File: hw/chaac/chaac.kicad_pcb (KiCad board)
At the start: 2 copper layers, 68.5 x 45.5 mm, 61 parts, among them J1 windrain, J2 Conn_02x08_Odd_Even, J3 Conn_02x08_Odd_Even, J4 AM2315, J5 Battery, J6 Solar Panel, J7 UART, Q1 Q_PMOS_GSD, SW1 RST, SW2 RST, U1 MIC550X, U2 BMP280, U3 MCP73871

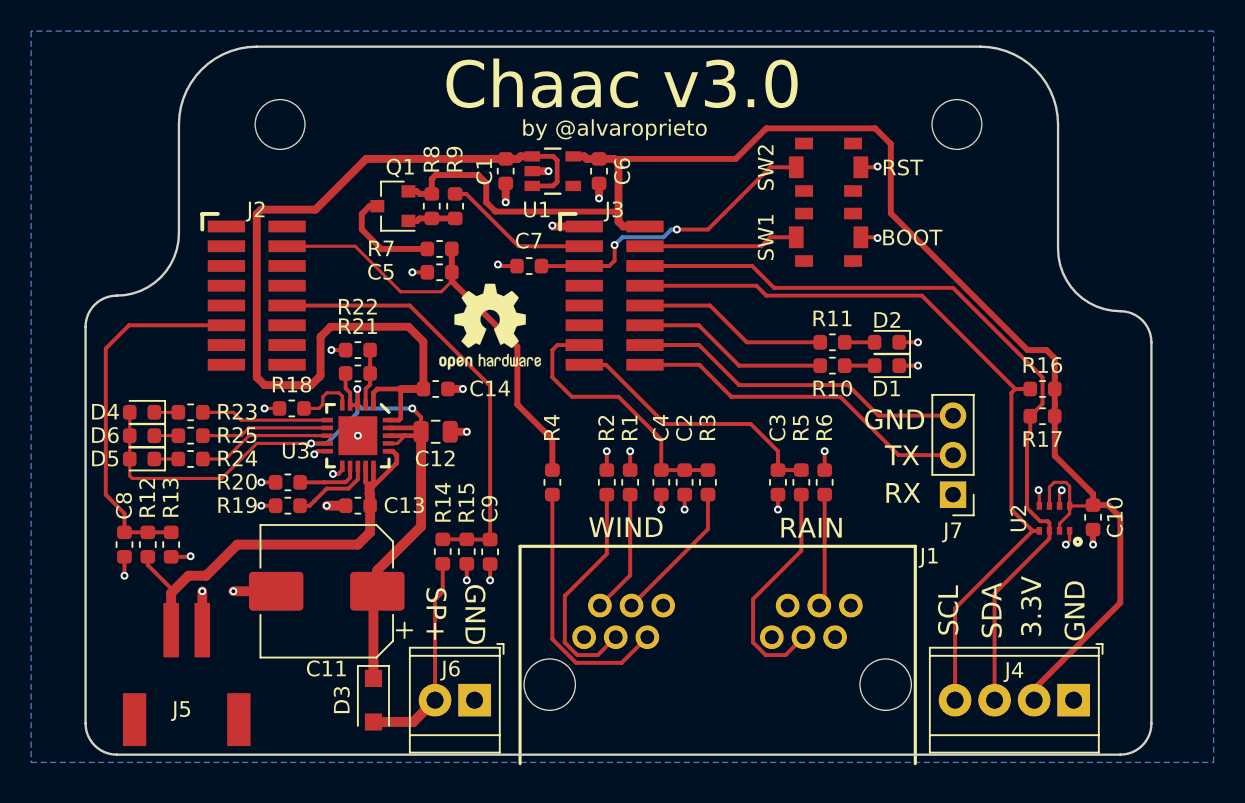
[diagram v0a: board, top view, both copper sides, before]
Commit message: Released chaac v3.1 to OSHPark
Moved NRF52 back into chaac pcb.
Removed external T/H connector, switched to BME280 for temp, humidity,
and pressure sensing.

Using RP-SMA connector for this version.
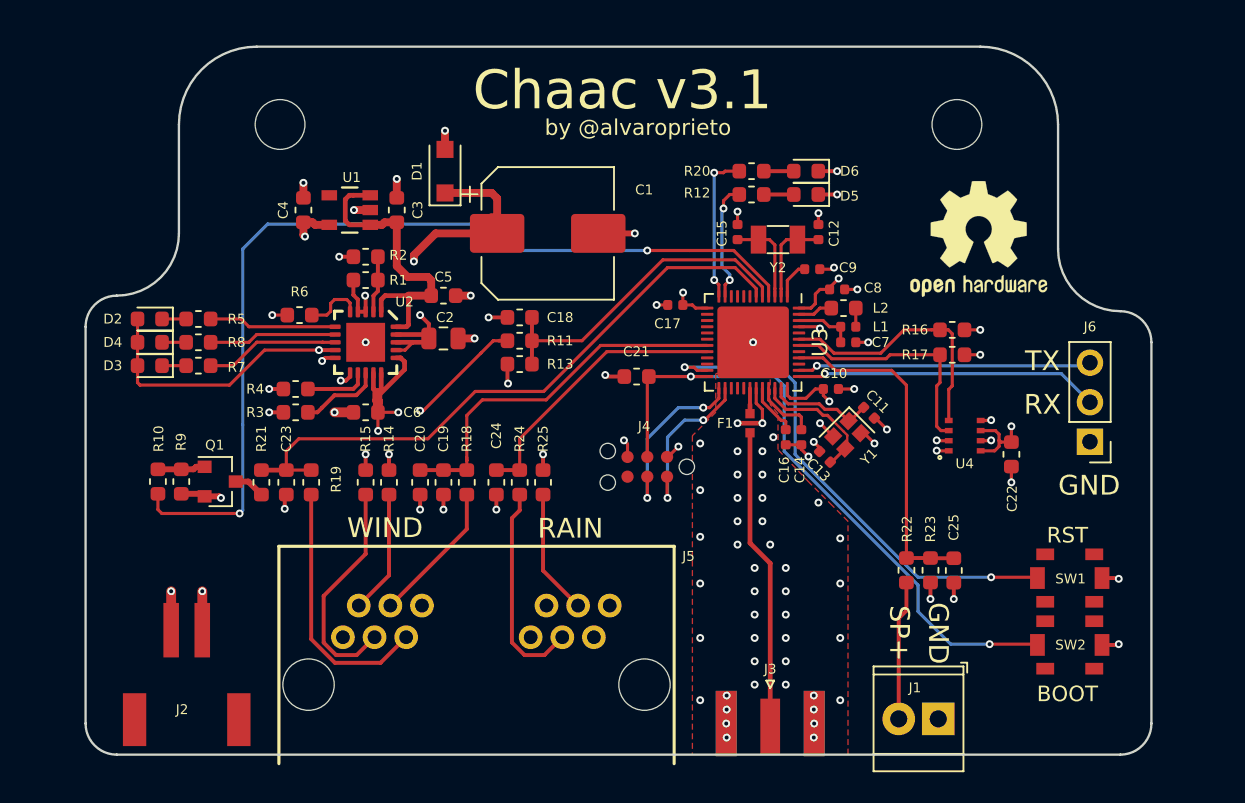
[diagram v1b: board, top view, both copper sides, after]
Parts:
- removed the J2 at (123.5, 91.0)
- removed the REF** at (138.5, 93.0)
- removed the U2 at (174.8, 105.3)
- added C10: 0.1uF, Capacitor_SMD:C_0402_1005Metric, F.Cu at (160.4, 97.0)
- added C11: 12pF, Capacitor_SMD:C_0402_1005Metric, F.Cu at (162.8, 98.5)
- added C12: 12pF, Capacitor_SMD:C_0402_1005Metric, F.Cu at (159.6, 86.9)
- added C13: 12pF, Capacitor_SMD:C_0402_1005Metric, F.Cu at (160.0, 101.4)
- added C14: 100pF, Capacitor_SMD:C_0402_1005Metric, F.Cu at (158.5, 100.1)
- added C15: 12pF, Capacitor_SMD:C_0402_1005Metric, F.Cu at (154.4, 86.9)
- added C16: DNP, Capacitor_SMD:C_0402_1005Metric, F.Cu at (157.5, 100.1)
- added C17: 0.1uF, Capacitor_SMD:C_0402_1005Metric, F.Cu at (150.4, 91.6)
- added C7: 1uF, Capacitor_SMD:C_0402_1005Metric, F.Cu at (161.5, 94.0)
- added C8: 4.7uF, Capacitor_SMD:C_0402_1005Metric, F.Cu at (160.8, 90.6)
- added C9: 0.1uF, Capacitor_SMD:C_0402_1005Metric, F.Cu at (159.2, 89.3)
- added F1: 2450FM07A0029T, alvarop:2450FM07A0029T, F.Cu at (155.2, 99.2)
- added L1: 15nH, Inductor_SMD:L_0402_1005Metric, F.Cu at (161.5, 93.0)
- added L2: 10uH, Inductor_SMD:L_0603_1608Metric, F.Cu at (161.2, 91.8)
- added REF**: OSHW-Logo2_9.8x8mm_SilkScreen, Symbol:OSHW-Logo2_9.8x8mm_SilkScreen, F.Cu at (169.9, 87.3)
- added U3: NRF52811-QFAA, alvarop:NRF52811-QFN48, F.Cu at (155.4, 94.0)
- added U4: BME280, alvarop:BME280, F.Cu at (169.0, 100.0)
- added Y1: 32MHz, Crystal:Crystal_SMD_2016-4Pin_2.0x1.6mm, F.Cu at (161.4, 99.9)
- added Y2: 32.768kHz, Crystal:Crystal_SMD_3215-2Pin_3.2x1.5mm, F.Cu at (157.0, 87.4)
- J3: value Conn_02x08_Odd_Even -> Conn_Coaxial; footprint alvarop:20021121-00016C4LF -> Connector_Coaxial:SMA_Samtec_SMA-J-P-H-ST-EM1_EdgeMount
- J4: value AM2315 -> TC2030-CTX; footprint TerminalBlock_TE-Connectivity:TerminalBlock_TE_282834-4_1x04_P2.54mm_Horizontal -> alvarop:TC2030-NL
- R3: renamed from R19; value 2k -> 33k
- moved SW2 34.4 mm to (175.8, 113.5)
- moved D1 34.3 mm to (135.6, 83.0), turned to 90 degrees
- moved J4 31.2 mm to (148.6, 102.0)
- moved C25 29.8 mm to (168.3, 108.7)
- moved J1 29.8 mm to (167.3, 118.2)
- moved R22 29.8 mm to (165.3, 108.7)
- moved R23 29.8 mm to (166.8, 108.7)
- moved C18 29.3 mm to (140.4, 92.4), turned to 180 degrees
- moved J3 29.3 mm to (156.5, 118.5)
- moved R11 27.3 mm to (140.4, 93.9), turned to 180 degrees
- moved C1 27.0 mm to (142.2, 87.0), turned to 0 degrees
- moved SW1 26.8 mm to (175.8, 109.2)
- moved R10 26.0 mm to (117.2, 103.0), turned to 90 degrees
- moved R13 25.2 mm to (140.4, 95.4), turned to 0 degrees
- moved R9 23.9 mm to (118.7, 103.0), turned to 270 degrees
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- renumbered C11 to C1, C8 to C18, C2 to C19, C12 to C2, C4 to C20, C7 to C21, C10 to C22, C5 to C23, C3 to C24, C9 to C25, C1 to C3, C6 to C4, C14 to C5, C13 to C6, D3 to D1, D4 to D2, D5 to D3, D6 to D4, D1 to D5, D2 to D6, J6 to J1, J5 to J2, J1 to J5, J7 to J6, R21 to R1, R9 to R10, R12 to R11, R10 to R12, R1 to R14, R2 to R15, R3 to R18, R4 to R19, R22 to R2, R11 to R20, R7 to R21, R14 to R22, R15 to R23, R5 to R24, R6 to R25, R20 to R4, R23 to R5, R18 to R6, R24 to R7, R25 to R8, R8 to R9, U3 to U2
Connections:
- J3 pad 1: GND -> /ANT
- J3 pad 2: +3V3 -> GND
- J4 pad 1: GND -> +3V3
- J4 pad 2: +3V3 -> /SWDIO
- J4 pad 3: /SDA -> /nRST
- J4 pad 4: /SCL -> /SWDCLK
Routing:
- net +3V3: track 96.9 -> 24.6 mm, vias 0 -> 10
- net /SNS_3V3_EN: track 9.69 -> 60.3 mm, vias 0 -> 2
- net /VIN: track 58.7 -> 19.8 mm
- net /SDA: track 52.0 -> 15.1 mm
- net /SCL: track 50.7 -> 16.6 mm
- net /BOOT: track 9.96 -> 32.5 mm, vias 0 -> 2
- net /nRST: track 19.6 -> 41.8 mm
- net /ANT: track 0.00 -> 19.4 mm
- net GND: track 41.3 -> 55.2 mm, vias 36 -> 94
- net /MCP_VIN: track 55.0 -> 41.5 mm, vias 3 -> 4
- net /WDIR: track 29.0 -> 40.6 mm
- net /SWDCLK: track 0.00 -> 11.5 mm, vias 0 -> 2
- net /SWDIO: track 0.00 -> 10.7 mm, vias 0 -> 2
- net /VBATT: track 29.1 -> 20.1 mm, vias 0 -> 4
- net Net-(C13-Pad1): track 0.00 -> 8.43 mm
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- added copper zone on PWR, net +3V3
- added copper zone on PWR, net /MCP_VIN
- added copper zone on PWR, net /SOLAR_IN
- added copper zone on PWR, net /VBATT
- added copper zone on F.Cu, net GND
- added copper zone on GND, net GND
- removed copper zone on B.Cu, net GND
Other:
- copper layers 2 -> 4
- rule solder_mask_min_width: 0.25 -> 0.1016
- rule trace_min: 0.1524 -> 0.0889
- board text added: "Chaac v3.1"
- board text removed: "3.3V"
- board text removed: "Chaac v3.0"
- board text removed: "SCL"
- board text removed: "SDA"

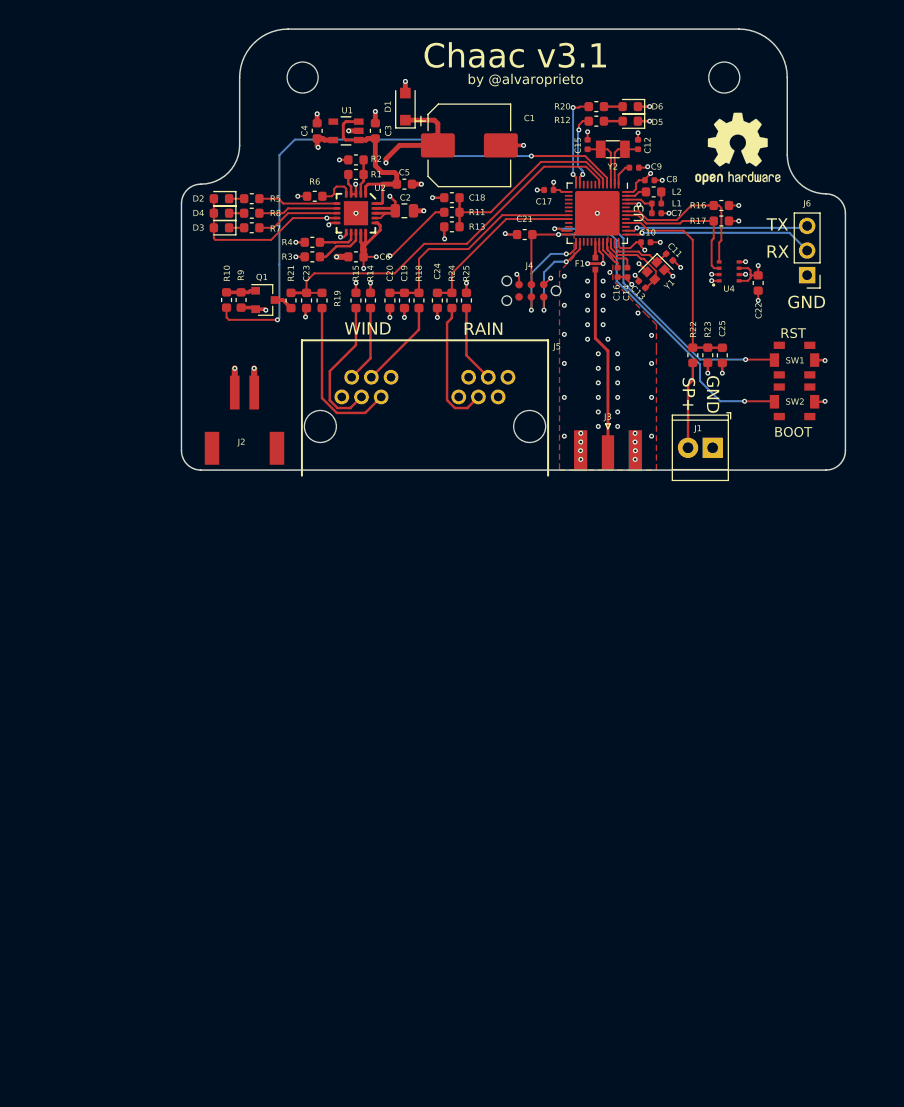
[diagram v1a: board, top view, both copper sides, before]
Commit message: Started chaac v4.0 Schematic + layout
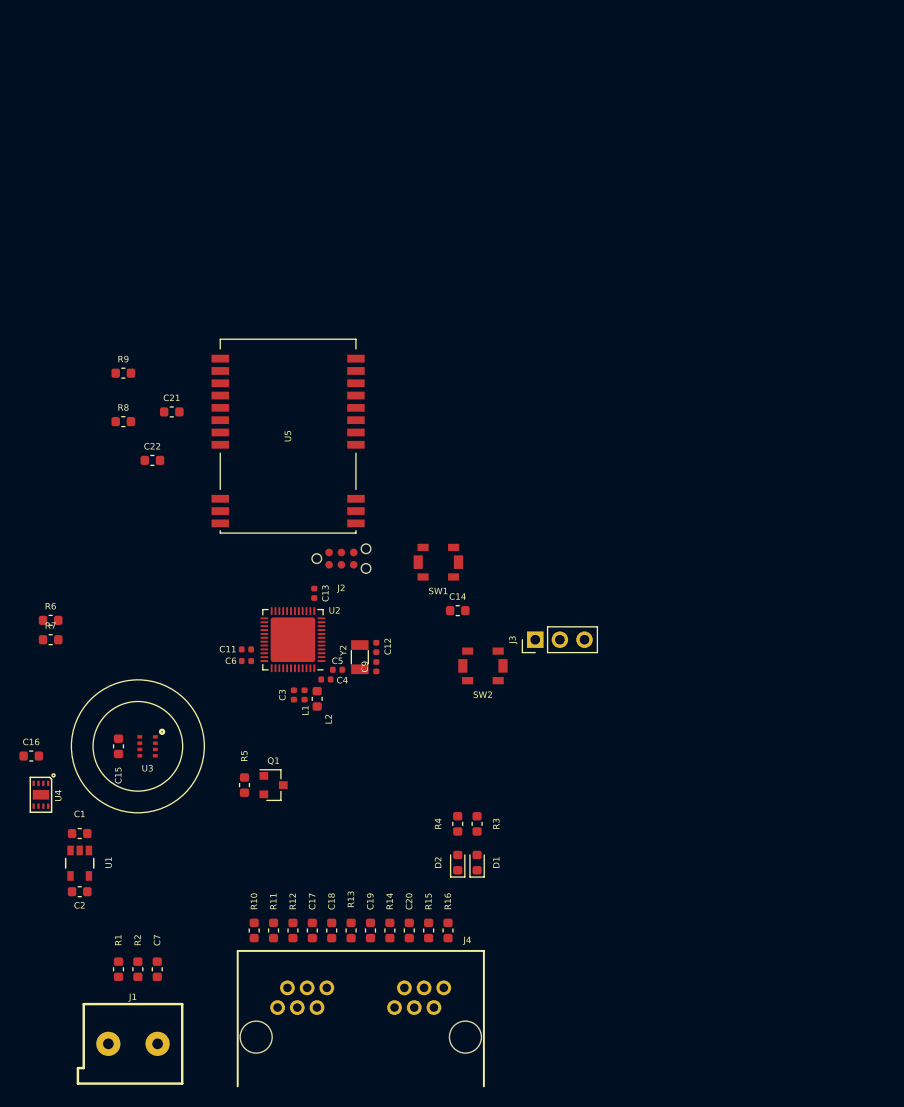
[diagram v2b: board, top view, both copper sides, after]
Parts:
- removed C10: 0.1uF, Capacitor_SMD:C_0402_1005Metric
- removed C23, C24, C25: 0.1uF, Capacitor_SMD:C_0603_1608Metric
- removed C8: 4.7uF, Capacitor_SMD:C_0402_1005Metric
- removed D3, D4, D5, D6: LED_ALT, LED_SMD:LED_0603_1608Metric
- removed F1: 2450FM07A0029T, alvarop:2450FM07A0029T
- removed J5: windrain, alvarop:043814-6621
- removed J6: UART, Connector_PinHeader_2.54mm:PinHeader_1x03_P2.54mm_Vertical
- removed R17, R21: 4.7k, Resistor_SMD:R_0603_1608Metric
- removed R18, R19, R24, R25: 1k, Resistor_SMD:R_0603_1608Metric
- removed R20: 10k, Resistor_SMD:R_0603_1608Metric
- removed R22, R23: 100k, Resistor_SMD:R_0603_1608Metric
- removed REF**: OSHW-Logo2_9.8x8mm_SilkScreen, Symbol:OSHW-Logo2_9.8x8mm_SilkScreen
- removed REF** (x2): MountingHole_3.2mm_M3, MountingHole:MountingHole_3.2mm_M3
- removed Y1: 32MHz, Crystal:Crystal_SMD_2016-4Pin_2.0x1.6mm
- added U5: E22-X00M22S, alvarop:E22-X00M22S, F.Cu at (130.5, 126.0)
- C1: value 470uF -> 1uF; footprint Capacitor_SMD:CP_Elec_8x10 -> Capacitor_SMD:C_0603_1608Metric
- C11: value 12pF -> 100pF
- C13: value 12pF -> 0.1uF
- C14: value 100pF -> 0.1uF; footprint Capacitor_SMD:C_0402_1005Metric -> Capacitor_SMD:C_0603_1608Metric
- C15: value 12pF -> 0.1uF; footprint Capacitor_SMD:C_0402_1005Metric -> Capacitor_SMD:C_0603_1608Metric
- C16: value DNP -> 0.1uF; footprint Capacitor_SMD:C_0402_1005Metric -> Capacitor_SMD:C_0603_1608Metric
- C17: value 0.1uF -> 0.01 uF; footprint Capacitor_SMD:C_0402_1005Metric -> Capacitor_SMD:C_0603_1608Metric
- C18: value 0.1uF -> 0.01 uF
- C19, C20: value 0.01 uF -> 0.1uF
- C2: value 10uF -> 1uF; footprint Capacitor_SMD:C_0805_2012Metric -> Capacitor_SMD:C_0603_1608Metric
- C22: value 0.1uF -> 1uF
- C3: footprint Capacitor_SMD:C_0603_1608Metric -> Capacitor_SMD:C_0402_1005Metric
- C4: value 1uF -> 4.7uF; footprint Capacitor_SMD:C_0603_1608Metric -> Capacitor_SMD:C_0402_1005Metric
- C5, C6: value 4.7uF -> 0.1uF; footprint Capacitor_SMD:C_0603_1608Metric -> Capacitor_SMD:C_0402_1005Metric
- C7: value 1uF -> 0.1uF; footprint Capacitor_SMD:C_0402_1005Metric -> Capacitor_SMD:C_0603_1608Metric
- C9: value 0.1uF -> 12pF
- D1: value MBR120VLSFT1G -> LED_ALT; footprint Diode_SMD:D_SOD-123F -> LED_SMD:LED_0603_1608Metric
- J1: value Solar Panel -> Battery; footprint TerminalBlock_TE-Connectivity:TerminalBlock_TE_282834-2_1x02_P2.54mm_Horizontal -> alvarop:‎282837-2‎
- J2: value Battery -> TC2030-CTX; footprint alvarop:S2B-PH-SM4-TB -> alvarop:TC2030-NL
- J3: value Conn_Coaxial -> UART; footprint Connector_Coaxial:SMA_Samtec_SMA-J-P-H-ST-EM1_EdgeMount -> Connector_PinHeader_2.54mm:PinHeader_1x03_P2.54mm_Vertical
- J4: value TC2030-CTX -> windrain; footprint alvarop:TC2030-NL -> alvarop:043814-6621
- R1: value 270k -> 100k
- R10: value 0 -> 1k
- R11, R13: value 100k -> 1k
- R12: value 10k -> 1k
- R14: value 1k -> 4.7k
- R16: value 4.7k -> 1k
- R3: value 33k -> 10k
- R4: value 100k -> 10k
- R6, R7: value 10k -> 4.7k
- R8, R9: value 10k -> 0
- U1: value MIC550X -> TPS7A0530PDBVT
- U2: value MCP73871 -> NRF52811-QFAA; footprint alvarop:MCP73871 -> alvarop:NRF52811-QFN48
- U3: value NRF52811-QFAA -> BMP280; footprint alvarop:NRF52811-QFN48 -> alvarop:BMP280
- U4: value BME280 -> SHT3x-DIS; footprint alvarop:BME280 -> alvarop:SHT3x
- moved C7 93.5 mm to (110.0, 172.0), turned to 270 degrees
- moved U4 89.2 mm to (98.0, 154.0), turned to 270 degrees
- moved R12 89.2 mm to (124.0, 168.0), turned to 270 degrees
- moved R2 86.5 mm to (108.0, 172.0), turned to 90 degrees
- moved J1 85.8 mm to (107.5, 179.7), turned to 0 degrees
- moved R1 85.6 mm to (106.0, 172.0), turned to 270 degrees
- moved C1 81.6 mm to (102.0, 158.0), turned to 180 degrees
- moved U1 80.4 mm to (102.0, 161.1), turned to 0 degrees
- moved C17 80.2 mm to (126.0, 168.0), turned to 270 degrees
- moved R16 79.9 mm to (140.0, 168.0), turned to 90 degrees
- moved J4 79.0 mm to (131.0, 179.0), turned to 0 degrees
- moved C15 78.7 mm to (106.0, 149.0), turned to 270 degrees
- moved C16 78.4 mm to (97.0, 150.0), turned to 0 degrees
- moved D1 78.4 mm to (143.0, 161.0)
- moved C2 77.8 mm to (102.0, 164.0), turned to 180 degrees
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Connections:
- C1 pad 1: /MCP_VIN -> /VBATT
- C11 pad 1: GND -> Net-(C11-Pad1)
- C11 pad 2: Net-(C11-Pad2) -> GND
- C13 pad 1: Net-(C13-Pad1) -> GND
- C13 pad 2: GND -> +3V3
- C14 pad 1: Net-(C14-Pad1) -> /nRST
- C15 pad 1: Net-(C15-Pad1) -> +3V3
- C16 pad 1: Net-(C16-Pad1) -> +3V3
- C17 pad 1: GND -> /WSPEED
- C17 pad 2: +3V3 -> GND
- C18 pad 1: /BATT -> /WSPEED
- C19 pad 1: /WSPEED -> /WDIR
- C2 pad 1: /MCP_VIN -> +3V3
- C20 pad 1: /WSPEED -> GND
- C20 pad 2: GND -> /RAIN
- C21 pad 1: /nRST -> Net-(C21-Pad1)
- C22 pad 1: +3V3 -> Net-(C21-Pad1)
- C3 pad 1: /VIN -> GND
- C3 pad 2: GND -> Net-(C3-Pad2)
- C4 pad 1: +3V3 -> GND
- C4 pad 2: GND -> +3V3
- C5 pad 1: /VIN -> GND
- C5 pad 2: GND -> Net-(C5-Pad2)
- C6 pad 1: /VBATT -> GND
- C6 pad 2: GND -> +3V3
- C7 pad 1: GND -> /BATT
- C7 pad 2: Net-(C7-Pad2) -> GND
- C9 pad 1: GND -> Net-(C9-Pad1)
- C9 pad 2: Net-(C9-Pad2) -> GND
- D1 pad 1: /MCP_VIN -> GND
- D1 pad 2: /SOLAR_IN -> Net-(D1-Pad2)
- D2 pad 1: Net-(D2-Pad1) -> GND
- D2 pad 2: /MCP_VIN -> Net-(D2-Pad2)
- J1 pad 1: GND -> /VBATT
- J1 pad 2: /SOLAR_IN -> GND
- J2 pad 1: /VBATT -> +3V3
- J2 pad 2: GND -> /SWDIO
- J3 pad 1: /ANT -> GND
- J3 pad 2: GND -> /UART_RX
- J4 pad 1: +3V3 -> Net-(J4-Pad1)
- J4 pad 2: /SWDIO -> Net-(J4-Pad2)
- J4 pad 3: /nRST -> Net-(J4-Pad3)
- J4 pad 4: /SWDCLK -> Net-(J4-Pad4)
- J4 pad 5: GND -> Net-(J4-Pad5)
- L1 pad 1: Net-(C7-Pad2) -> Net-(C3-Pad2)
- Q1 pad 1: Net-(Q1-Pad1) -> /SNS_3V3_EN
- R1 pad 1: Net-(R1-Pad1) -> /BATT
- R1 pad 2: /MCP_VIN -> /VBATT
- R10 pad 1: /SNS_3V3_EN -> GND
- R10 pad 2: Net-(Q1-Pad1) -> Net-(J4-Pad2)
- R11 pad 1: /BATT -> GND
- R11 pad 2: /VBATT -> Net-(J4-Pad3)
- R12 pad 1: Net-(D5-Pad2) -> /WSPEED
- R12 pad 2: /LED1 -> Net-(J4-Pad4)
- R13 pad 1: GND -> Net-(J4-Pad5)
- R13 pad 2: /BATT -> /WDIR
- R14 pad 1: GND -> /WDIR
- R14 pad 2: Net-(J5-Pad2) -> /SNS_3V3
- R15 pad 1: GND -> /RAIN
- R15 pad 2: Net-(J5-Pad3) -> Net-(J4-Pad9)
- R16 pad 1: /SCL -> Net-(J4-Pad10)
- R16 pad 2: +3V3 -> GND
- R2 pad 2: Net-(R1-Pad1) -> /BATT
- R3 pad 1: GND -> Net-(D1-Pad2)
- R3 pad 2: Net-(R3-Pad2) -> /LED1
- R4 pad 1: GND -> Net-(D2-Pad2)
- R4 pad 2: Net-(R4-Pad2) -> /LED2
- R5 pad 1: Net-(R5-Pad1) -> /SNS_3V3_EN
- R5 pad 2: Net-(D2-Pad1) -> +3V3
- R6 pad 1: Net-(R6-Pad1) -> /SCL
- R6 pad 2: GND -> +3V3
- R7 pad 1: Net-(R7-Pad1) -> /SDA
- R7 pad 2: Net-(D3-Pad1) -> +3V3
- R8 pad 1: Net-(R8-Pad1) -> Net-(C21-Pad1)
- R8 pad 2: Net-(D4-Pad1) -> +3V3
- R9 pad 1: Net-(Q1-Pad1) -> Net-(C21-Pad1)
- R9 pad 2: +3V3 -> /SNS_3V3
- U1 pad 1: /VIN -> /VBATT
- U1 pad 3: /VIN -> /VBATT
- U2 pad 1: /VIN -> Net-(C5-Pad2)
- U2 pad 10: GND -> /UART_TX
- U2 pad 11: GND -> /LED1
- U2 pad 12: Net-(R4-Pad2) -> /LED2
- U2 pad 13: Net-(R3-Pad2) -> +3V3
- U2 pad 14: /VBATT -> /E22_DIO1
- U2 pad 15: /VBATT -> /E22_BUSY
- U2 pad 16: /VBATT -> /E22_NRST
- U2 pad 17: /MCP_VIN -> /MISO
- U2 pad 18: /MCP_VIN -> /MOSI
- U2 pad 19: /MCP_VIN -> /SCK
- U2 pad 2: Net-(R1-Pad1) -> Net-(C9-Pad1)
- U2 pad 20: /VIN -> /E22_NSS
- U2 pad 21: GND -> /E22_RXEN
- U2 pad 3: /MCP_VIN -> Net-(C12-Pad1)
- U2 pad 4: /MCP_VIN -> Net-(U2-Pad4)
- U2 pad 5: Net-(R6-Pad1) -> Net-(U2-Pad5)
- U2 pad 6: Net-(R5-Pad1) -> Net-(U2-Pad6)
- U2 pad 7: Net-(R8-Pad1) -> /SDA
- U2 pad 8: Net-(R7-Pad1) -> /SCL
- U2 pad 9: /MCP_VIN -> /UART_RX
- U3 pad 1: Net-(C9-Pad2) -> GND
- U3 pad 2: Net-(C12-Pad1) -> +3V3
- U3 pad 3: Net-(C15-Pad1) -> /SDA
- U3 pad 4: /SNS_3V3_EN -> /SCL
- U3 pad 5: /BATT -> GND
- U3 pad 6: /WDIR -> +3V3
- U3 pad 7: Net-(U3-Pad7) -> GND
- U3 pad 8: Net-(U3-Pad8) -> +3V3
- U4 pad 1: GND -> /SDA
- U4 pad 2: +3V3 -> GND
- U4 pad 3: /SDA -> Net-(U4-Pad3)
- U4 pad 5: GND -> +3V3
- U4 pad 6: +3V3 -> Net-(U4-Pad6)
- U4 pad 8: +3V3 -> GND
- Y2 pad 1: Net-(C12-Pad1) -> Net-(C9-Pad1)
- Y2 pad 2: Net-(C15-Pad1) -> Net-(C12-Pad1)
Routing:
- net /SNS_3V3_EN: track 60.3 -> 0.00 mm, vias 2 -> 0
- net GND: track 55.2 -> 0.00 mm, vias 94 -> 0
- net /nRST: track 41.8 -> 0.00 mm, vias 2 -> 0
- net /MCP_VIN: track 41.5 -> 0.00 mm, vias 4 -> 0
- net /WDIR: track 40.6 -> 0.00 mm
- net /BOOT: track 32.5 -> 0.00 mm, vias 2 -> 0
- net +3V3: track 24.6 -> 0.00 mm, vias 10 -> 0
- net /WSPEED: track 24.0 -> 0.00 mm
- net /VSOLAR: track 21.8 -> 0.00 mm
- net /BATT: track 21.3 -> 0.00 mm
- net /VBATT: track 20.1 -> 0.00 mm, vias 4 -> 0
- net /VIN: track 19.8 -> 0.00 mm
- net /UART_RX: track 19.5 -> 0.00 mm, vias 1 -> 0
- net /ANT: track 19.4 -> 0.00 mm
- net /UART_TX: track 18.9 -> 0.00 mm, vias 1 -> 0
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- removed copper zone on PWR, net +3V3
- removed copper zone on PWR, net /MCP_VIN
- removed copper zone on PWR, net /SOLAR_IN
- removed copper zone on PWR, net /VBATT
- removed copper zone on F.Cu, net GND
- removed copper zone on GND, net GND
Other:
- board outline removed
- board text removed: "BOOT"
- board text removed: "Chaac v3.1"
- board text removed: "GND"
- board text removed: "RAIN"
- board text removed: "RST"
- board text removed: "RX"
- board text removed: "SP+"
- board text removed: "TX"
- board text removed: "WIND"
- board text removed: "by @alvaroprieto"
- board text removed: "https://github.com/alvarop/chaac"

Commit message: Finished chaac v4.0!
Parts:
- added REF**: OSHW-Logo_28.5x30mm_SilkScreen, Symbol:OSHW-Logo_28.5x30mm_SilkScreen, B.Cu at (124.4, 151.0)
- added REF**: MountingHole_3.2mm_M3, MountingHole:MountingHole_3.2mm_M3, F.Cu at (141.0, 133.0)
- added REF**: MountingHole_3.2mm_M3, MountingHole:MountingHole_3.2mm_M3, F.Cu at (107.0, 133.0)
- J1: footprint alvarop:‎282837-2‎ -> TerminalBlock_TE-Connectivity:TerminalBlock_TE_282834-2_1x02_P2.54mm_Horizontal
- U2: footprint alvarop:NRF52811-QFN48 -> alvarop:NRF52811-QFN48-VIAS
- moved C16 54.6 mm to (142.0, 180.9)
- moved U4 50.2 mm to (141.9, 178.3)
- moved R9 48.5 mm to (107.5, 159.0), turned to 270 degrees
- moved R6 46.6 mm to (141.5, 155.2), turned to 180 degrees
- moved R7 46.5 mm to (141.5, 156.9), turned to 180 degrees
- moved R8 43.5 mm to (105.5, 159.0), turned to 270 degrees
- moved SW1 40.7 mm to (106.5, 154.5)
- moved SW2 38.2 mm to (106.5, 150.0)
- moved C21 30.2 mm to (109.6, 144.6), turned to 90 degrees
- moved J2 29.9 mm to (112.8, 154.8), turned to 270 degrees
- moved C14 29.3 mm to (117.5, 152.5), turned to 180 degrees
- moved C15 29.2 mm to (135.0, 145.8)
- moved U3 28.5 mm to (137.3, 146.0)
- moved C22 25.2 mm to (111.2, 144.6), turned to 90 degrees
- moved J3 18.7 mm to (131.5, 131.5), turned to 0 degrees
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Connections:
- J1 pad 1: /VBATT -> GND
- J1 pad 2: GND -> /VBATT
- U2 pad 10: /UART_TX -> /SCL
- U2 pad 11: /LED1 -> /UART_RX
- U2 pad 12: /LED2 -> /UART_TX
- U2 pad 38: /RAIN -> Net-(U2-Pad38)
- U2 pad 39: /WSPEED -> Net-(U2-Pad39)
- U2 pad 40: /WDIR -> /BATT
- U2 pad 41: /BATT -> /WSPEED
- U2 pad 42: Net-(U2-Pad42) -> /WDIR
- U2 pad 43: Net-(U2-Pad43) -> /RAIN
- U2 pad 7: /SDA -> /LED2
- U2 pad 8: /SCL -> /LED1
- U2 pad 9: /UART_RX -> /SDA
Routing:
- net +3V3: track 0.00 -> 169.0 mm, vias 0 -> 2
- net GND: track 0.00 -> 58.2 mm, vias 0 -> 45
- net /SDA: track 0.00 -> 54.5 mm, vias 0 -> 3
- net /SCL: track 0.00 -> 50.6 mm, vias 0 -> 3
- net /SNS_3V3: track 0.00 -> 48.9 mm, vias 0 -> 4
- net /UART_RX: track 0.00 -> 24.3 mm, vias 0 -> 2
- net /VBATT: track 0.00 -> 23.0 mm
- net /RAIN: track 0.00 -> 21.5 mm
- net Net-(C21-Pad1): track 0.00 -> 20.7 mm
- net /WDIR: track 0.00 -> 20.6 mm
- net /UART_TX: track 0.00 -> 19.9 mm, vias 0 -> 2
- net /nRST: track 0.00 -> 19.4 mm, vias 0 -> 2
- net /BOOT: track 0.00 -> 18.6 mm, vias 0 -> 2
- net /E22_RXEN: track 0.00 -> 17.7 mm
- net /E22_TXEN: track 0.00 -> 16.7 mm
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- added copper zone on B.Cu, net GND
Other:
- board outline added: 42 x 55 mm
- copper layers 4 -> 2
- rule trace_min: 0.0889 -> 0.1524
- board text added: "(3-5.5V)"
- board text added: "+"
- board text added: "-"
- board text added: "<--Temperature/Humidity"
- board text added: "BATT"
- board text added: "Chaac"
- board text added: "DFU"
- board text added: "GND"
- board text added: "Pressure"
- board text added: "RAIN"
- board text added: "RST"
- board text added: "RX"
- board text added: "TX"
- board text added: "WIND"
- board text added: "by @alvaroprieto"
- board text added: "https://chaac.network"
- board text added: "https://github.com/alvarop/chaac/"
- board text added: "v4.0"
